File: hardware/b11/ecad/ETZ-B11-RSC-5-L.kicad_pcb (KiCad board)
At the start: 2 copper layers, 112.3 x 85.8 mm, 0 parts

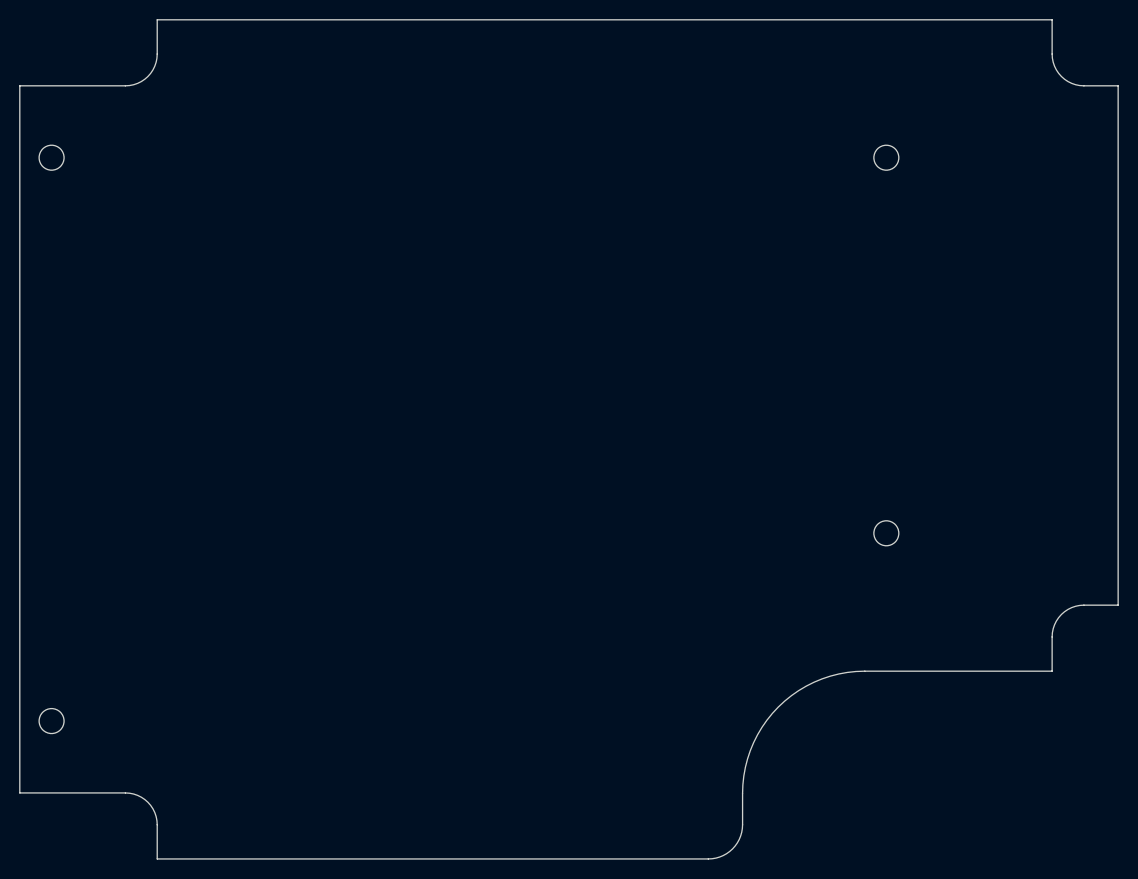
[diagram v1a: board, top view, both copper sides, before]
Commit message: feat(hardware/b11): place hotswap sockets on all carrier boards, south-facing
- Place Kailh MX hotswap sockets (MX-Hotswap-1U) on 4 normal-profile carrier
  boards at 19.2mm pitch, flipped to B.Cu, 180° south-facing orientation
- Place Kailh Choc v1 hotswap sockets (PG1350) on 4 low-profile carrier boards
  at 19.2mm pitch, 180° south-facing orientation
- Add 3D model (Kailh-Choc-Socket-CPG135001S30.step) to PG1350 footprint with
  correct offset/rotation for B.Cu-pad, F.Cu-module placement
- Strip F.SilkS, F.Fab, F.CrtYd top-layer graphics from LP carrier PG1350 footprints
- Rename place-b11-switches.py → place-b11-switches-np.py for symmetry with new lp script
- Add place-b11-switches-lp.py for Choc v1 placement automation

Co-Authored-By: Claude Sonnet 4.6 <noreply@anthropic.com>
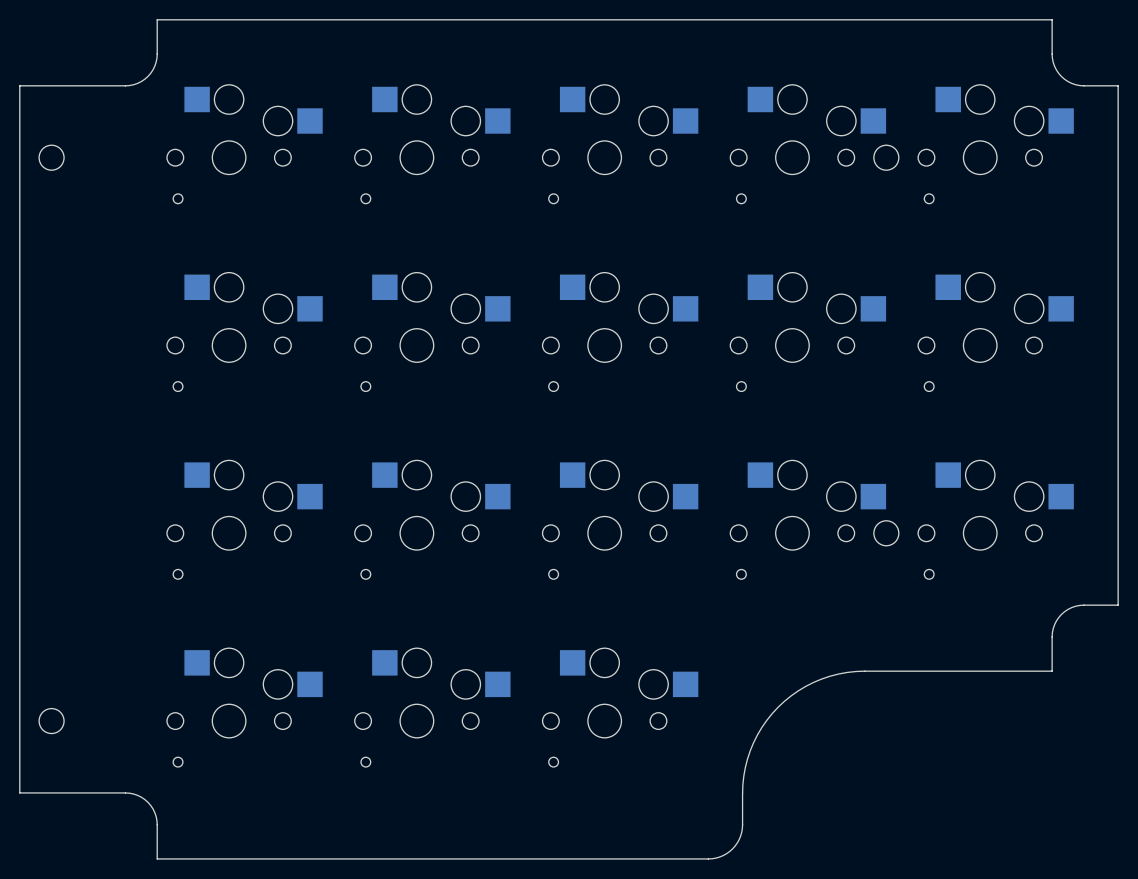
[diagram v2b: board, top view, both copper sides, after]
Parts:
- added SW1: Kailh_socket_PG1350, Kailh_socket_PG1350, F.Cu at (190.6, 73.3)
- added SW10: Kailh_socket_PG1350, Kailh_socket_PG1350, F.Cu at (113.8, 92.5)
- added SW11: Kailh_socket_PG1350, Kailh_socket_PG1350, F.Cu at (190.6, 111.7)
- added SW12: Kailh_socket_PG1350, Kailh_socket_PG1350, F.Cu at (171.3, 111.7)
- added SW13: Kailh_socket_PG1350, Kailh_socket_PG1350, F.Cu at (152.2, 111.7)
- added SW14: Kailh_socket_PG1350, Kailh_socket_PG1350, F.Cu at (132.9, 111.7)
- added SW15: Kailh_socket_PG1350, Kailh_socket_PG1350, F.Cu at (113.8, 111.7)
- added SW16: Kailh_socket_PG1350, Kailh_socket_PG1350, F.Cu at (152.2, 130.9)
- added SW17: Kailh_socket_PG1350, Kailh_socket_PG1350, F.Cu at (132.9, 130.9)
- added SW18: Kailh_socket_PG1350, Kailh_socket_PG1350, F.Cu at (113.8, 130.9)
- added SW2: Kailh_socket_PG1350, Kailh_socket_PG1350, F.Cu at (171.3, 73.3)
- added SW3: Kailh_socket_PG1350, Kailh_socket_PG1350, F.Cu at (152.2, 73.3)
- added SW4: Kailh_socket_PG1350, Kailh_socket_PG1350, F.Cu at (132.9, 73.3)
- added SW5: Kailh_socket_PG1350, Kailh_socket_PG1350, F.Cu at (113.8, 73.3)
- added SW6: Kailh_socket_PG1350, Kailh_socket_PG1350, F.Cu at (190.6, 92.5)
- added SW7: Kailh_socket_PG1350, Kailh_socket_PG1350, F.Cu at (171.3, 92.5)
- added SW8: Kailh_socket_PG1350, Kailh_socket_PG1350, F.Cu at (152.2, 92.5)
- added SW9: Kailh_socket_PG1350, Kailh_socket_PG1350, F.Cu at (132.9, 92.5)

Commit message: feat(hardware/b11): add SMD 6028 back-mount LED footprint and place on all carrier PCBs
- Add LED_SMD_6028_BackMount footprint with router-safe rounded-rectangle
  slot cutout (3.3 × 3.9 mm, 0.5 mm corners, 1 mm bit), roundrect pads
  (1.4 × 2.8 mm, 25% ratio), silkscreen polarity markers clear of pads
- Add LED_SMD_6028.step 3D model from 3D Content Central
- Add place-b11-leds.py: places 18–22 LEDs per carrier PCB aligned to
  the switch grid, 5.9 mm south of each switch center
- Place LEDs on all 8 carrier PCBs (LSC/RSC × 5/6-col × N/L)

Co-Authored-By: Claude Sonnet 4.6 <noreply@anthropic.com>
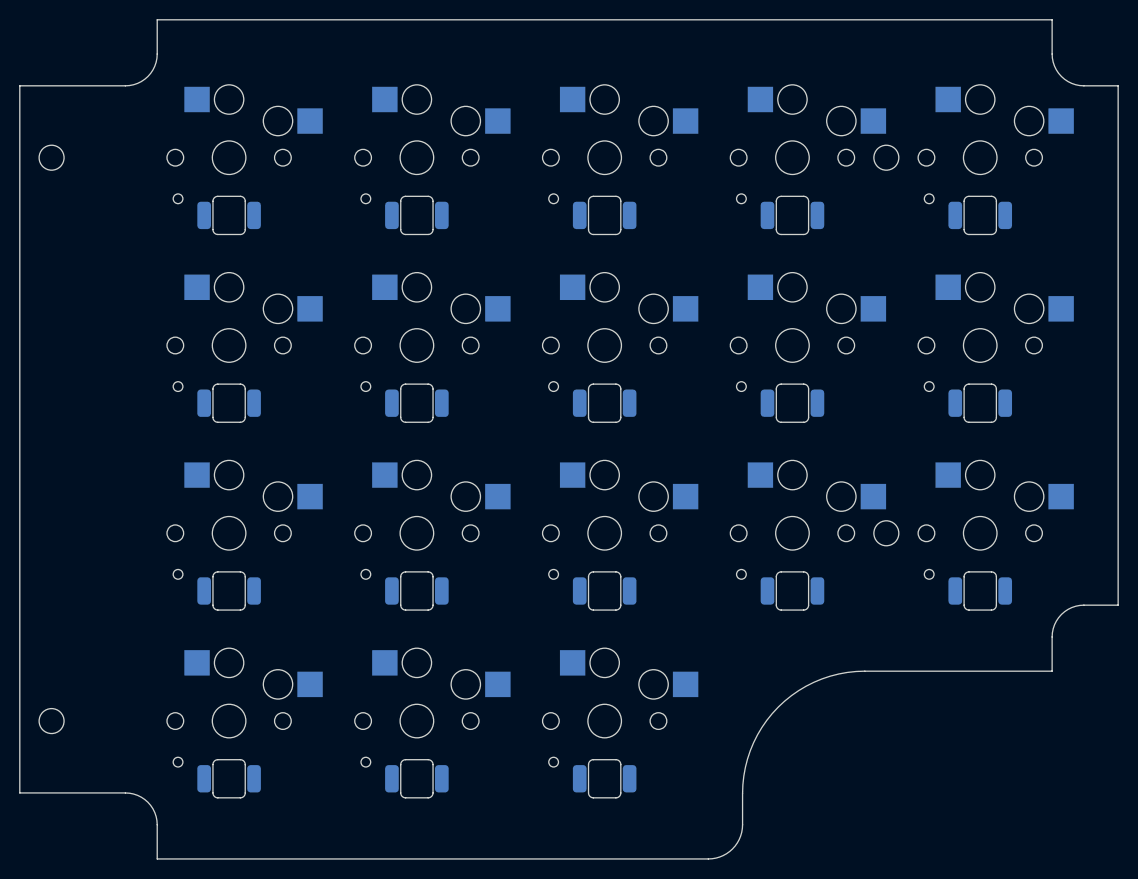
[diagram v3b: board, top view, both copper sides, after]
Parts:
- added LED1: LED_SMD_6028_BackMount, LED_SMD_6028_BackMount, B.Cu at (190.6, 79.2)
- added LED10: LED_SMD_6028_BackMount, LED_SMD_6028_BackMount, B.Cu at (113.8, 98.4)
- added LED11: LED_SMD_6028_BackMount, LED_SMD_6028_BackMount, B.Cu at (190.6, 117.6)
- added LED12: LED_SMD_6028_BackMount, LED_SMD_6028_BackMount, B.Cu at (171.3, 117.6)
- added LED13: LED_SMD_6028_BackMount, LED_SMD_6028_BackMount, B.Cu at (152.2, 117.6)
- added LED14: LED_SMD_6028_BackMount, LED_SMD_6028_BackMount, B.Cu at (132.9, 117.6)
- added LED15: LED_SMD_6028_BackMount, LED_SMD_6028_BackMount, B.Cu at (113.8, 117.6)
- added LED16: LED_SMD_6028_BackMount, LED_SMD_6028_BackMount, B.Cu at (152.2, 136.8)
- added LED17: LED_SMD_6028_BackMount, LED_SMD_6028_BackMount, B.Cu at (132.9, 136.8)
- added LED18: LED_SMD_6028_BackMount, LED_SMD_6028_BackMount, B.Cu at (113.8, 136.8)
- added LED2: LED_SMD_6028_BackMount, LED_SMD_6028_BackMount, B.Cu at (171.3, 79.2)
- added LED3: LED_SMD_6028_BackMount, LED_SMD_6028_BackMount, B.Cu at (152.2, 79.2)
- added LED4: LED_SMD_6028_BackMount, LED_SMD_6028_BackMount, B.Cu at (132.9, 79.2)
- added LED5: LED_SMD_6028_BackMount, LED_SMD_6028_BackMount, B.Cu at (113.8, 79.2)
- added LED6: LED_SMD_6028_BackMount, LED_SMD_6028_BackMount, B.Cu at (190.6, 98.4)
- added LED7: LED_SMD_6028_BackMount, LED_SMD_6028_BackMount, B.Cu at (171.3, 98.4)
- added LED8: LED_SMD_6028_BackMount, LED_SMD_6028_BackMount, B.Cu at (152.2, 98.4)
- added LED9: LED_SMD_6028_BackMount, LED_SMD_6028_BackMount, B.Cu at (132.9, 98.4)

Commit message: fix(hardware/b11): fix switch socket placement, 3D models, and submodule pins
- Pin MX_V2 submodule to ab59b57 (before upstream "topside pads" change that
  moved SMD pads to F.Cu — old commit has correct B.Cu pads natively)
- Fix SWIG type-registry corruption in both switch placement scripts by
  pre-loading all footprint instances and caching pad refs before LoadBoard()
- Fix LP script: add make_patched_lib to rewrite Choc socket 3D model path
  to absolute path and convert old (at ...) inch offset to (offset ...) mm
  format — KiCad 9 was multiplying the old format by 25.4, placing model
  127mm off-center
- Regenerate all 8 carrier PCBs with updated board outlines (LSC-6 mounting
  hole positions) and correctly placed switches + LEDs

Co-Authored-By: Claude Sonnet 4.6 <noreply@anthropic.com>
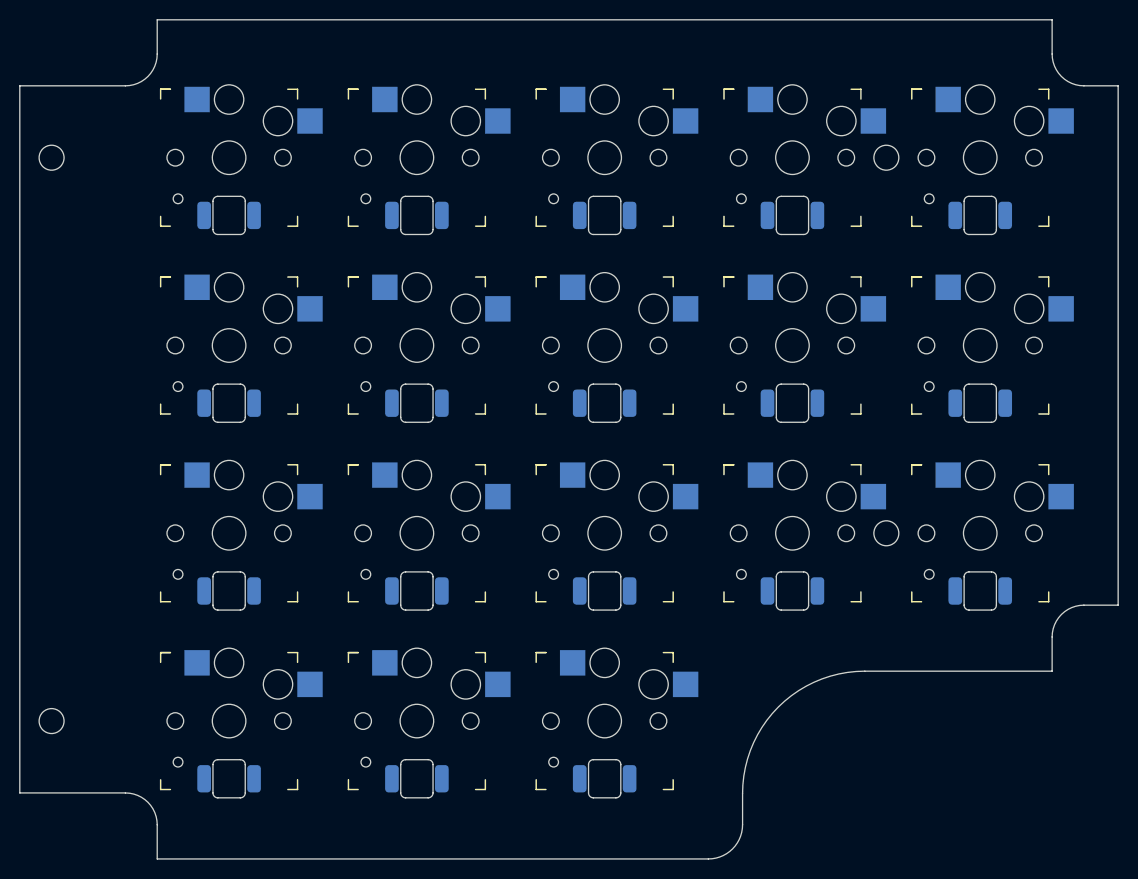
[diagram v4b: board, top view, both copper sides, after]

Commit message: fix(hardware/b11): adjust LED offset to 5.0mm and regenerate all carrier PCBs
Reduces south-facing LED offset from 5.9mm to 5.0mm (closer to the
standard 5.08mm switch-to-LED spacing). All 8 carrier PCBs regenerated.

Co-Authored-By: Claude Sonnet 4.6 <noreply@anthropic.com>
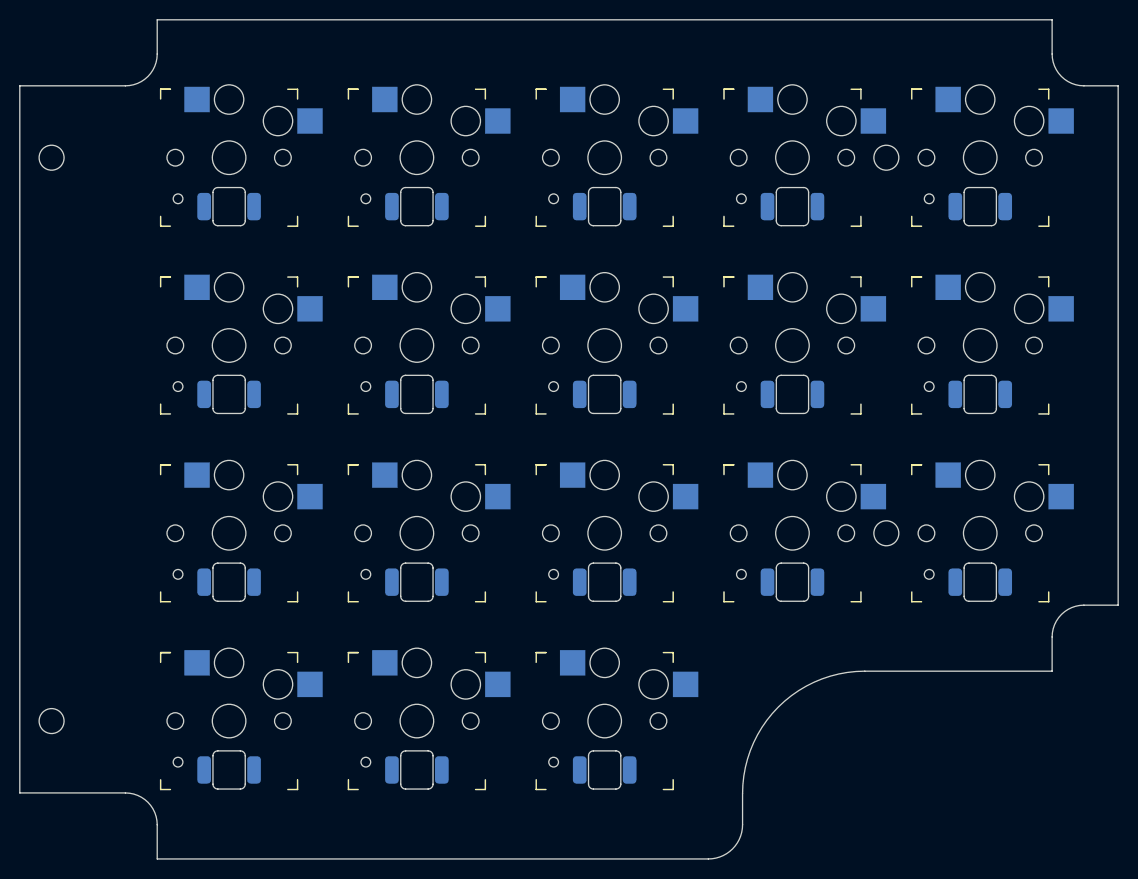
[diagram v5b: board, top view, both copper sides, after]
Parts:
- moved LED11 0.90 mm to (190.6, 116.7)
- moved LED12 0.90 mm to (171.3, 116.7)
- moved LED13 0.90 mm to (152.2, 116.7)
- moved LED14 0.90 mm to (132.9, 116.7)
- moved LED15 0.90 mm to (113.8, 116.7)
- moved LED1 0.90 mm to (190.6, 78.3)
- moved LED10 0.90 mm to (113.8, 97.5)
- moved LED16 0.90 mm to (152.2, 135.9)
- moved LED17 0.90 mm to (132.9, 135.9)
- moved LED18 0.90 mm to (113.8, 135.9)
- moved LED2 0.90 mm to (171.3, 78.3)
- moved LED3 0.90 mm to (152.2, 78.3)
- moved LED4 0.90 mm to (132.9, 78.3)
- moved LED5 0.90 mm to (113.8, 78.3)
- moved LED6 0.90 mm to (190.6, 97.5)
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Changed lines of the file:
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@@
 	(footprint "LED_SMD_6028_BackMount"
 		(layer "B.Cu")
-		(at 171.35 98.4)
+		(at 171.35 97.5)
 		(descr "SMD 6028 back-paste reverse-mount LED, 5.88x2.80mm body, 3.20mm lens, slot 3.3x6.2mm")
 		(tags "LED SMD 6028 reverse-mount back-paste backlighting Choc")
@@
 	(footprint "LED_SMD_6028_BackMount"
 		(layer "B.Cu")
-		(at 113.75 79.2)
+		(at 152.15 78.3)
 		(descr "SMD 6028 back-paste reverse-mount LED, 5.88x2.80mm body, 3.20mm lens, slot 3.3x6.2mm")
 		(tags "LED SMD 6028 reverse-mount back-paste backlighting Choc")
-		(property "Reference" "LED5"
+		(property "Reference" "LED3"
 			(at 0 -2 0)
 			(layer "B.Fab")
@@
 	(footprint "LED_SMD_6028_BackMount"
 		(layer "B.Cu")
-		(at 132.95 136.799999)
+		(at 132.95 116.699999)
 		(descr "SMD 6028 back-paste reverse-mount LED, 5.88x2.80mm body, 3.20mm lens, slot 3.3x6.2mm")
 		(tags "LED SMD 6028 reverse-mount back-paste backlighting Choc")
-		(property "Reference" "LED17"
+		(property "Reference" "LED14"
 			(at 0 -2 0)
 			(layer "B.Fab")
@@
 	(footprint "LED_SMD_6028_BackMount"
 		(layer "B.Cu")
-		(at 132.95 117.6)
+		(at 190.55 97.5)
 		(descr "SMD 6028 back-paste reverse-mount LED, 5.88x2.80mm body, 3.20mm lens, slot 3.3x6.2mm")
 		(tags "LED SMD 6028 reverse-mount back-paste backlighting Choc")
-		(property "Reference" "LED14"
+		(property "Reference" "LED6"
 			(at 0 -2 0)
 			(layer "B.Fab")
@@
 	(footprint "LED_SMD_6028_BackMount"
 		(layer "B.Cu")
-		(at 190.55 117.6)
+		(at 152.15 135.899999)
 		(descr "SMD 6028 back-paste reverse-mount LED, 5.88x2.80mm body, 3.20mm lens, slot 3.3x6.2mm")
 		(tags "LED SMD 6028 reverse-mount back-paste backlighting Choc")
-		(property "Reference" "LED11"
+		(property "Reference" "LED16"
 			(at 0 -2 0)
 			(layer "B.Fab")
@@
 	(footprint "LED_SMD_6028_BackMount"
 		(layer "B.Cu")
-		(at 171.35 117.6)
+		(at 190.55 78.3)
 		(descr "SMD 6028 back-paste reverse-mount LED, 5.88x2.80mm body, 3.20mm lens, slot 3.3x6.2mm")
 		(tags "LED SMD 6028 reverse-mount back-paste backlighting Choc")
-		(property "Reference" "LED12"
+		(property "Reference" "LED1"
 			(at 0 -2 0)
 			(layer "B.Fab")
@@
 	(footprint "LED_SMD_6028_BackMount"
 		(layer "B.Cu")
-		(at 152.15 117.6)
+		(at 152.15 116.699999)
 		(descr "SMD 6028 back-paste reverse-mount LED, 5.88x2.80mm body, 3.20mm lens, slot 3.3x6.2mm")
 		(tags "LED SMD 6028 reverse-mount back-paste backlighting Choc")
@@
 	(footprint "LED_SMD_6028_BackMount"
 		(layer "B.Cu")
-		(at 113.75 117.6)
+		(at 113.75 97.5)
 		(descr "SMD 6028 back-paste reverse-mount LED, 5.88x2.80mm body, 3.20mm lens, slot 3.3x6.2mm")
 		(tags "LED SMD 6028 reverse-mount back-paste backlighting Choc")
-		(property "Reference" "LED15"
+		(property "Reference" "LED10"
 			(at 0 -2 0)
 			(layer "B.Fab")
@@
 	(footprint "LED_SMD_6028_BackMount"
 		(layer "B.Cu")
-		(at 152.15 98.4)
+		(at 171.35 78.3)
 		(descr "SMD 6028 back-paste reverse-mount LED, 5.88x2.80mm body, 3.20mm lens, slot 3.3x6.2mm")
 		(tags "LED SMD 6028 reverse-mount back-paste backlighting Choc")
-		(property "Reference" "LED8"
+		(property "Reference" "LED2"
 			(at 0 -2 0)
 			(layer "B.Fab")
@@
 	(footprint "LED_SMD_6028_BackMount"
 		(layer "B.Cu")
-		(at 152.15 136.799999)
+		(at 113.75 78.3)
 		(descr "SMD 6028 back-paste reverse-mount LED, 5.88x2.80mm body, 3.20mm lens, slot 3.3x6.2mm")
 		(tags "LED SMD 6028 reverse-mount back-paste backlighting Choc")
-		(property "Reference" "LED16"
+		(property "Reference" "LED5"
 			(at 0 -2 0)
 			(layer "B.Fab")
@@
 	(footprint "LED_SMD_6028_BackMount"
 		(layer "B.Cu")
-		(at 132.95 79.2)
+		(at 152.15 97.5)
 		(descr "SMD 6028 back-paste reverse-mount LED, 5.88x2.80mm body, 3.20mm lens, slot 3.3x6.2mm")
 		(tags "LED SMD 6028 reverse-mount back-paste backlighting Choc")
-		(property "Reference" "LED4"
+		(property "Reference" "LED8"
 			(at 0 -2 0)
 			(layer "B.Fab")
@@
 	(footprint "LED_SMD_6028_BackMount"
 		(layer "B.Cu")
-		(at 190.55 79.2)
+		(at 190.55 116.699999)
 		(descr "SMD 6028 back-paste reverse-mount LED, 5.88x2.80mm body, 3.20mm lens, slot 3.3x6.2mm")
 		(tags "LED SMD 6028 reverse-mount back-paste backlighting Choc")
-		(property "Reference" "LED1"
+		(property "Reference" "LED11"
 			(at 0 -2 0)
 			(layer "B.Fab")
@@
 	(footprint "LED_SMD_6028_BackMount"
 		(layer "B.Cu")
-		(at 152.15 79.2)
+		(at 171.35 116.699999)
 		(descr "SMD 6028 back-paste reverse-mount LED, 5.88x2.80mm body, 3.20mm lens, slot 3.3x6.2mm")
 		(tags "LED SMD 6028 reverse-mount back-paste backlighting Choc")
-		(property "Reference" "LED3"
+		(property "Reference" "LED12"
 			(at 0 -2 0)
 			(layer "B.Fab")
@@
 	(footprint "LED_SMD_6028_BackMount"
 		(layer "B.Cu")
-		(at 171.35 79.2)
+		(at 132.95 78.3)
 		(descr "SMD 6028 back-paste reverse-mount LED, 5.88x2.80mm body, 3.20mm lens, slot 3.3x6.2mm")
 		(tags "LED SMD 6028 reverse-mount back-paste backlighting Choc")
-		(property "Reference" "LED2"
+		(property "Reference" "LED4"
 			(at 0 -2 0)
 			(layer "B.Fab")
@@
 	(footprint "LED_SMD_6028_BackMount"
 		(layer "B.Cu")
-		(at 113.75 136.799999)
+		(at 113.75 135.899999)
 		(descr "SMD 6028 back-paste reverse-mount LED, 5.88x2.80mm body, 3.20mm lens, slot 3.3x6.2mm")
 		(tags "LED SMD 6028 reverse-mount back-paste backlighting Choc")
@@
 	(footprint "LED_SMD_6028_BackMount"
 		(layer "B.Cu")
-		(at 190.55 98.4)
+		(at 132.95 97.5)
 		(descr "SMD 6028 back-paste reverse-mount LED, 5.88x2.80mm body, 3.20mm lens, slot 3.3x6.2mm")
 		(tags "LED SMD 6028 reverse-mount back-paste backlighting Choc")
-		(property "Reference" "LED6"
+		(property "Reference" "LED9"
 			(at 0 -2 0)
 			(layer "B.Fab")
@@
 	(footprint "LED_SMD_6028_BackMount"
 		(layer "B.Cu")
-		(at 113.75 98.4)
+		(at 113.75 116.699999)
 		(descr "SMD 6028 back-paste reverse-mount LED, 5.88x2.80mm body, 3.20mm lens, slot 3.3x6.2mm")
 		(tags "LED SMD 6028 reverse-mount back-paste backlighting Choc")
-		(property "Reference" "LED10"
+		(property "Reference" "LED15"
 			(at 0 -2 0)
 			(layer "B.Fab")
@@
 	(footprint "LED_SMD_6028_BackMount"
 		(layer "B.Cu")
-		(at 132.95 98.4)
+		(at 132.95 135.899999)
 		(descr "SMD 6028 back-paste reverse-mount LED, 5.88x2.80mm body, 3.20mm lens, slot 3.3x6.2mm")
 		(tags "LED SMD 6028 reverse-mount back-paste backlighting Choc")
-		(property "Reference" "LED9"
+		(property "Reference" "LED17"
 			(at 0 -2 0)
 			(layer "B.Fab")
